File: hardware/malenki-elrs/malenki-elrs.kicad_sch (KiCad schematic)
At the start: 19 parts, among them J1 Conn_01x02_Male-Connector, J2 Conn_01x08_Male, J3 Conn_01x02, U2 AP2210N-3.3TRG1, U3 ATtiny1616-M, U8 ESP32-C3FH4

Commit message: Finalised initial SX1280 schematics, started ESP32 schematic, replace Vreg in schematic
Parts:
- removed C4: 100nF, Capacitor_SMD:C_0402_1005Metric_Pad0.74x0.62mm_HandSolder, symbol malenki-nano-rescue:C-Device
- removed R6: 470R, Resistor_SMD:R_0402_1005Metric, symbol malenki-nano-rescue:R-Device
- removed R7, R8: 10k, Resistor_SMD:R_0402_1005Metric, symbol malenki-nano-rescue:R-Device
- removed U2: AP2210N-3.3TRG1, Package_TO_SOT_SMD:SOT-23, symbol mal_nano:HT7233
- removed U3: ATtiny1616-M, Package_DFN_QFN:VQFN-20-1EP_3x3mm_P0.4mm_EP1.7x1.7mm, symbol MCU_Microchip_ATtiny:ATtiny1616-M
- added C10: 1uF, Capacitor_SMD:C_0402_1005Metric, symbol Device:C
- added C11: 10uF, Capacitor_SMD:C_0402_1005Metric, symbol Device:C
- added C12: 100nF, Capacitor_SMD:C_0402_1005Metric, symbol Device:C
- added C9: 10nF, Capacitor_SMD:C_0402_1005Metric, symbol Device:C
- added R10, R9: 10k, Resistor_SMD:R_0402_1005Metric, symbol malenki-nano-rescue:R-Device
- added R11, R12: 470R, Resistor_SMD:R_0402_1005Metric, symbol malenki-nano-rescue:R-Device
- added U1: SPX3819M5-L-3-3, malenki-nano:SOT95P280X145-5N, symbol malenki-elrs:SPX3819M5-L-3-3
- R5: value 470R -> 499; LCSC C25117 -> C11702; Manufacturer (none) -> Uniroyal
- U8: footprint ESP32-C3FH4:QFN50P500X500X90-33N -> malenki-nano:QFN50P500X500X90-33N; LCSC (none) -> C2858491
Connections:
- net BLINKY: now also U8.6 (GPIO2)
- net GND: now also U8.33 (GND), C10.2, C11.2, C12.2, C9.2, R10.2, R9.2, U1.2 (GND)
- net VBAT: now also U1.1 (VIN), U1.3 (EN)
- net VLOGIC: now also U8.31 (VDDA), U8.32 (VDDA__1), C10.1, C11.1, C12.1, C9.1, U1.5 (VOUT)
- net W2: now also R11.2; no longer R5.2
- net W3: now also R12.2
- net WEAPON2: now also R11.1, R9.1; no longer R5.1
- net WEAPON3: now also R10.1, R12.1
- net ESP_MOSI: now reaches U8.10 (GPIO5/MTDI)
- net ESP_SCK: now reaches U8.12 (GPIO6/MTCK)
- net ESP_NSS: now reaches U8.13 (GPIO7/MTDO)
- net ESP_NRESET: now reaches U8.14 (GPIO8)
- net DIO1: now reaches U8.16 (GPIO10)
- net at U8.2 (VDD3P3): now also U8.3 (VDD3P3__1)
- net U0RXD: now reaches U8.27 (GPIO20/U0RXD)
- net at U8.28 (GPIO21/U0TXD): now also R5.1
- net BUSY: now reaches U8.8 (GPIO3)
- net ESP_MISO: now reaches U8.9 (GPIO4/MTMS)
- new net U0TXD: R5.2
- no-connect marks 5 -> 4
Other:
- sheet radio ports: added BUSY, DIO1, DIO2, DIO3; removed GIO1, RESET, SPI_SCK, SPI_SCS, SPI_SDIO
- note removed: "MCU"
- moved on the sheet: C2, C3, D1, D2, J1, R1, R2, R3, R4, U8

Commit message: Completed preliminary schematics
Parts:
- removed C12: 100nF, Capacitor_SMD:C_0402_1005Metric, symbol Device:C
- removed J2: Conn_01x08_Male, malenki-nano:SOIC_clipProgSmall, symbol Connector:Conn_01x08_Male
- added C10, C13, C4, C7, C9: 100nF, Capacitor_SMD:C_0402_1005Metric, symbol Device:C
- added C15: 1uF, Capacitor_SMD:C_0402_1005Metric, symbol Device:C
- added C2, C3: 12pF, Capacitor_SMD:C_0402_1005Metric, symbol Device:C
- added J2: PROG Header, Connector_PinHeader_1.27mm:PinHeader_2x03_P1.27mm_Vertical, symbol Connector_Generic:Conn_02x03_Odd_Even
- added R11, R14, R5: 470, Resistor_SMD:R_0402_1005Metric, symbol malenki-nano-rescue:R-Device
- added R13, R6: 10k, Resistor_SMD:R_0402_1005Metric, symbol malenki-nano-rescue:R-Device
- added Y1: ECS-400-10-37B2-CKY-TR, malenki-nano:XTAL_ECS-400-10-37B2-CKY-TR, symbol malenki-elrs:ECS-400-10-37B2-CKY-TR
- C6: renamed from C9; value 10nF -> 100nF
- J3: value Conn_01x02 -> Weapons
- R12: renamed from R5; value 499 -> 470
- R9: renamed from R1; value 470R -> 1k
- renumbered C2 to C1, C3 to C5, C10 to C8, R9 to R1, R2 to R10, R10 to R2, R11 to R3, R12 to R4, R3 to R7, R4 to R8, U8 to U2
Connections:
- net BLINKY: now also R9.2; no longer D1.2 (A)
- net GND: now also C10.2, C13.2, C15.2, C2.2, C3.2, C4.2, C7.2, C9.2, J2.4 (Pin_4), Y1.2, Y1.4; no longer R10.2, R9.2
- net MOTOR1F: now also U2.19 (GPIO12/SPIHD)
- net MOTOR1R: now also U2.20 (GPIO13/SPIWP)
- net MOTOR2F: now also U2.21 (GPIO14/SPICS0)
- net MOTOR2R: now also U2.22 (GPIO15/SPICLK)
- net MOTOR3F: now also U2.23 (GPIO16/SPID)
- net MOTOR3R: now also U2.24 (GPIO17/SPIQ)
- net TXDEBUG: now also R10.2, U2.25 (GPIO18/USB_D-); no longer D2.2 (A)
- net U0RXD: now also J2.5 (Pin_5), R11.2; no longer U2.27 (GPIO20/U0RXD)
- net U0TXD: now also J2.3 (Pin_3)
- net VLOGIC: now also D1.2 (A), D2.2 (A), U2.11 (VDD3P3_RTC), U2.17 (VDD3P3_CPU), U2.18 (VDD_SPI), U2.2 (VDD3P3), U2.3 (VDD3P3__1), C10.1, C13.1, C15.1, C7.1, C9.1, J2.2 (Pin_2), R13.2, R6.2
- net VSENSE: now also U2.26 (GPIO19/USB_D+)
- net W2: now also U2.4 (GPIO0/XTAL_32K_P)
- net W3: now also U2.5 (GPIO1/XTAL_32K_N)
- net at U2.15 (GPIO9): now also R13.1, R14.1
- net at U2.29 (XTAL_N): now also C2.1, Y1.1
- net at U2.30 (XTAL_P): now also C3.1, Y1.3
- net at U2.7 (CHIP_EN): now also C4.1, R5.2, R6.1
- new net: R11.1, U2.27 (GPIO20/U0RXD)
- new net ESPIO0: J2.6 (Pin_6), R14.2
- new net ESP_EN: J2.1 (Pin_1), R5.1
- no-connect marks 4 -> 2
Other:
- note added: "Bulk capacitor placed close to esp32"
- note removed: "Programming / diagnostic"
- moved on the sheet: C1, C5, C6, C8, D1, D2, J1, J3, R1, R10, R12, R2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

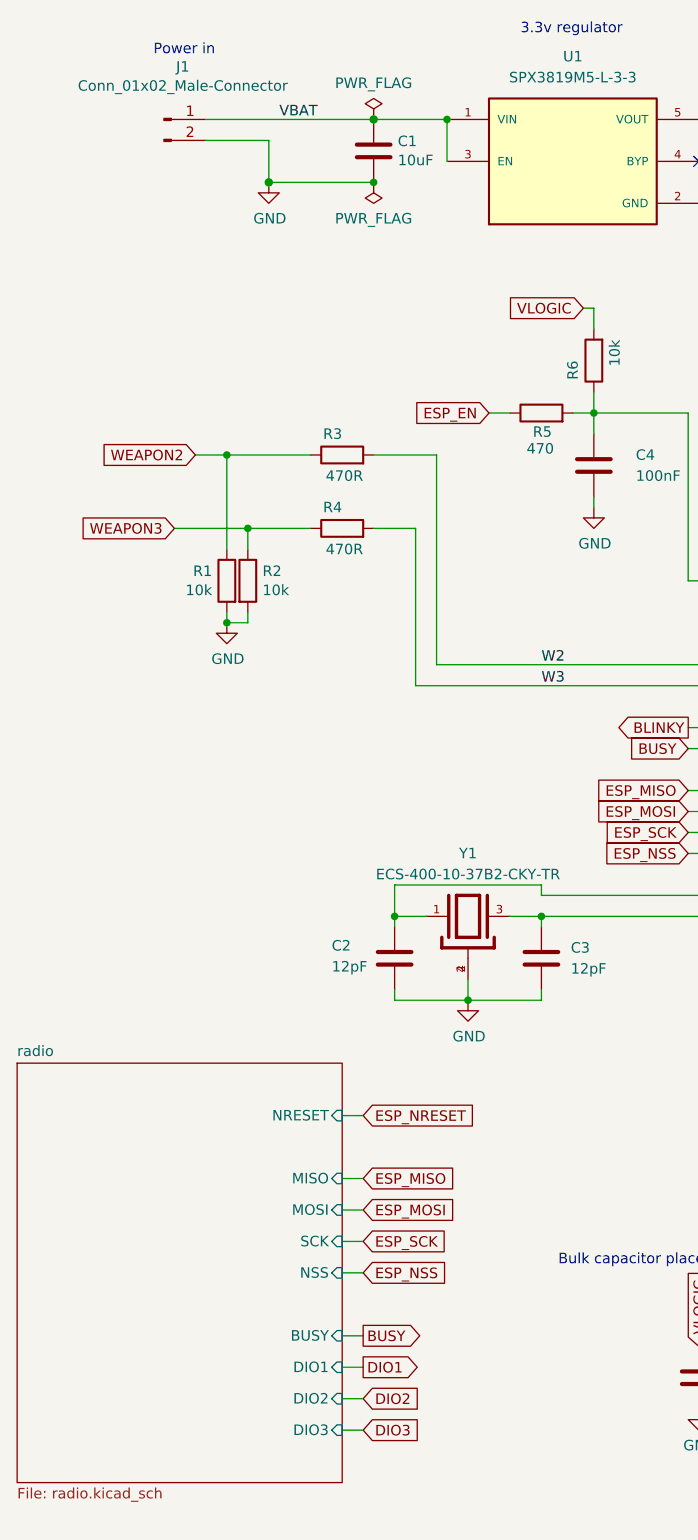
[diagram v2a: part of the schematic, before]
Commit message: Placing components for ESP and SX1280
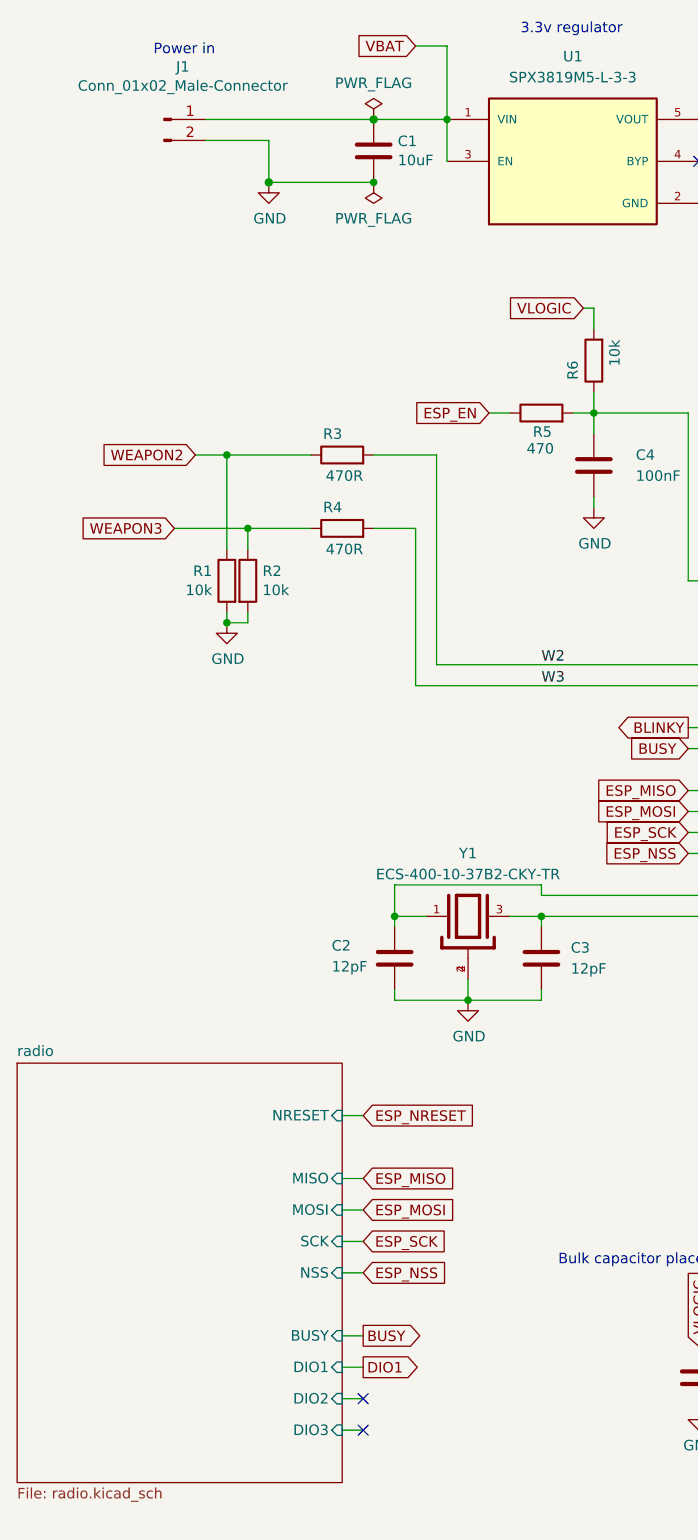
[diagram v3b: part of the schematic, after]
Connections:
- no-connect marks 2 -> 4
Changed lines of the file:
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@@
 		(at 100.33 88.9)
 	)
+	(no_connect
+		(at 58.42 186.69)
+	)
+	(no_connect
+		(at 58.42 182.88)
+	)
 	(wire
 		(pts
@@
 	(wire
 		(pts
-			(xy 39.37 27.94) (xy 59.69 27.94)
+			(xy 39.37 27.94) (xy 68.58 27.94)
 		)
 		(stroke
@@
 	(wire
 		(pts
+			(xy 64.77 19.05) (xy 68.58 19.05)
+		)
+		(stroke
+			(width 0)
+			(type solid)
+		)
+	)
+	(wire
+		(pts
 			(xy 156.21 83.82) (xy 179.07 83.82)
 		)
@@
 	(wire
 		(pts
-			(xy 59.69 27.94) (xy 68.58 27.94)
+			(xy 156.21 88.9) (xy 158.75 88.9)
+		)
+		(stroke
+			(width 0)
+			(type default)
+		)
+	)
+	(wire
+		(pts
+			(xy 162.56 48.26) (xy 162.56 46.99)
+		)
+		(stroke
+			(width 0)
+			(type default)
+		)
+	)
+	(wire
+		(pts
+			(xy 179.07 101.6) (xy 179.07 99.06)
+		)
+		(stroke
+			(width 0)
+			(type default)
+		)
+	)
+	(wire
+		(pts
+			(xy 179.07 109.22) (xy 179.07 111.76)
+		)
+		(stroke
+			(width 0)
+			(type default)
+		)
+	)
+	(wire
+		(pts
+			(xy 39.37 30.48) (xy 46.99 30.48)
 		)
 		(stroke
@@
 	(wire
 		(pts
-			(xy 156.21 88.9) (xy 158.75 88.9)
-		)
-		(stroke
-			(width 0)
-			(type default)
-		)
-	)
-	(wire
-		(pts
-			(xy 162.56 48.26) (xy 162.56 46.99)
-		)
-		(stroke
-			(width 0)
-			(type default)
-		)
-	)
-	(wire
-		(pts
-			(xy 179.07 101.6) (xy 179.07 99.06)
-		)
-		(stroke
-			(width 0)
-			(type default)
-		)
-	)
-	(wire
-		(pts
-			(xy 179.07 109.22) (xy 179.07 111.76)
-		)
-		(stroke
-			(width 0)
-			(type default)
-		)
-	)
-	(wire
-		(pts
-			(xy 39.37 30.48) (xy 46.99 30.48)
+			(xy 80.01 121.92) (xy 80.01 120.65)
+		)
+		(stroke
+			(width 0)
+			(type default)
+		)
+	)
+	(wire
+		(pts
+			(xy 99.06 27.94) (xy 104.14 27.94)
 		)
 		(stroke
@@
 	(wire
 		(pts
-			(xy 80.01 121.92) (xy 80.01 120.65)
-		)
-		(stroke
-			(width 0)
-			(type default)
-		)
-	)
-	(wire
-		(pts
-			(xy 99.06 27.94) (xy 104.14 27.94)
+			(xy 156.21 73.66) (xy 156.21 76.2)
+		)
+		(stroke
+			(width 0)
+			(type default)
+		)
+	)
+	(wire
+		(pts
+			(xy 156.21 104.14) (xy 158.75 104.14)
+		)
+		(stroke
+			(width 0)
+			(type default)
+		)
+	)
+	(wire
+		(pts
+			(xy 55.88 156.21) (xy 58.42 156.21)
+		)
+		(stroke
+			(width 0)
+			(type default)
+		)
+	)
+	(wire
+		(pts
+			(xy 62.23 133.35) (xy 62.23 134.62)
+		)
+		(stroke
+			(width 0)
+			(type default)
+		)
+	)
+	(wire
+		(pts
+			(xy 62.23 124.46) (xy 66.04 124.46)
+		)
+		(stroke
+			(width 0)
+			(type default)
+		)
+	)
+	(wire
+		(pts
+			(xy 41.91 68.58) (xy 41.91 80.01)
+		)
+		(stroke
+			(width 0)
+			(type default)
+		)
+	)
+	(wire
+		(pts
+			(xy 168.91 124.46) (xy 171.45 124.46)
+		)
+		(stroke
+			(width 0)
+			(type default)
+		)
+	)
+	(wire
+		(pts
+			(xy 165.1 63.5) (xy 162.56 63.5)
+		)
+		(stroke
+			(width 0)
+			(type default)
+		)
+	)
+	(wire
+		(pts
+			(xy 68.58 19.05) (xy 68.58 27.94)
 		)
 		(stroke
 			(width 0)
 			(type solid)
-		)
-	)
-	(wire
-		(pts
-			(xy 156.21 73.66) (xy 156.21 76.2)
-		)
-		(stroke
-			(width 0)
-			(type default)
-		)
-	)
-	(wire
-		(pts
-			(xy 156.21 104.14) (xy 158.75 104.14)
-		)
-		(stroke
-			(width 0)
-			(type default)
-		)
-	)
-	(wire
-		(pts
-			(xy 55.88 156.21) (xy 58.42 156.21)
-		)
-		(stroke
-			(width 0)
-			(type default)
-		)
-	)
-	(wire
-		(pts
-			(xy 62.23 133.35) (xy 62.23 134.62)
-		)
-		(stroke
-			(width 0)
-			(type default)
-		)
-	)
-	(wire
-		(pts
-			(xy 62.23 124.46) (xy 66.04 124.46)
-		)
-		(stroke
-			(width 0)
-			(type default)
-		)
-	)
-	(wire
-		(pts
-			(xy 41.91 68.58) (xy 41.91 80.01)
-		)
-		(stroke
-			(width 0)
-			(type default)
-		)
-	)
-	(wire
-		(pts
-			(xy 168.91 124.46) (xy 171.45 124.46)
-		)
-		(stroke
-			(width 0)
-			(type default)
-		)
-	)
-	(wire
-		(pts
-			(xy 165.1 63.5) (xy 162.56 63.5)
-		)
-		(stroke
-			(width 0)
-			(type default)
 		)
 	)
@@
 	(label "W2"
 		(at 80.01 93.98 0)
-		(effects
-			(font
-				(size 1.27 1.27)
-			)
-			(justify left bottom)
-		)
-	)
-	(label "VBAT"
-		(at 48.26 27.94 0)
 		(effects
 			(font
@@
 		)
 	)
-	(global_label "DIO3"
-		(shape input)
-		(at 58.42 186.69 0)
-		(fields_autoplaced yes)
-		(effects
-			(font
-				(size 1.27 1.27)
-			)
-			(justify left)
-		)
-		(property "Intersheetrefs" "${INTERSHEET_REFS}"
-			(at 65.9151 186.69 0)
-			(hide yes)
-			(show_name no)
-			(do_not_autoplace no)
-			(effects
-				(font
-					(size 1.27 1.27)
-				)
-				(justify left)
-			)
-		)
-	)
 	(global_label "VBAT"
 		(shape input)
@@
 		(property "Intersheetrefs" "${INTERSHEET_REFS}"
 			(at 125.73 160.1449 90)
-			(hide yes)
-			(show_name no)
-			(do_not_autoplace no)
-			(effects
-				(font
-					(size 1.27 1.27)
-				)
-				(justify left)
-			)
-		)
-	)
-	(global_label "DIO2"
-		(shape input)
-		(at 58.42 182.88 0)
-		(fields_autoplaced yes)
-		(effects
-			(font
-				(size 1.27 1.27)
-			)
-			(justify left)
-		)
-		(property "Intersheetrefs" "${INTERSHEET_REFS}"
-			(at 65.9151 182.88 0)
 			(hide yes)
 			(show_name no)
@@
 			)
 		)
+	)
+	(global_label "VBAT"
+		(shape input)
+		(at 64.77 19.05 180)
+		(fields_autoplaced yes)
+		(effects
+			(font
+				(size 1.27 1.27)
+			)
+			(justify right)
+		)
+		(property "Intersheetrefs" "${INTERSHEET_REFS}"
+			(at 57.2749 19.05 0)
+			(hide yes)
+			(show_name no)
+			(do_not_autoplace no)
+			(effects
+				(font
+					(size 1.27 1.27)
+				)
+				(justify right)
+			)
+		)

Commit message: minor changes ready for final checks
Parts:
- removed C11: 10uF, Capacitor_SMD:C_0402_1005Metric, symbol Device:C
- C10, C13, C4, C6, C7, C9: LCSC (none) -> C100072
- C15, C8: LCSC (none) -> C29266
- C2, C3: LCSC (none) -> C76948
- D1: LCSC C72041 -> C2986058; MPN 19-217/BHC-ZL1M2RY/3T -> 19-217/BHC-ZL1M2RY/6T
- D2: LCSC C2286 -> C2986060; MPN KT-0603R -> 19-217/R6C-AL1M2VY/6T; Manufacturer Hubei KENTO -> EVERLIGHT
- J2: now not fitted
- R1, R2, R8: LCSC C25744 -> C71617; Manufacturer Uniroyal -> VISHAY; Partnum C25804 -> CRCW040210K0FKED
- R11, R12, R14, R5: LCSC C11702 -> C25117; Manufacturer Uniroyal -> (none)
- R13, R6: LCSC C25117 -> C71617; Partnum (none) -> CRCW040210K0FKED
- R3: value 470R -> 470; Partnum (none) -> 0402WGF4700TCE
- R4: value 470R -> 470
- R9: LCSC C25117 -> C11702
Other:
- note removed: "Bulk capacitor placed close to esp32"
